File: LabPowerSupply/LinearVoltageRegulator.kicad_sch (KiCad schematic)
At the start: 16 parts, among them Q1_LVR1 PJA3404_R1_00001, Q2_LVR1 PJA3404_R1_00001, Q3_LVR1 PJA3404_R1_00001

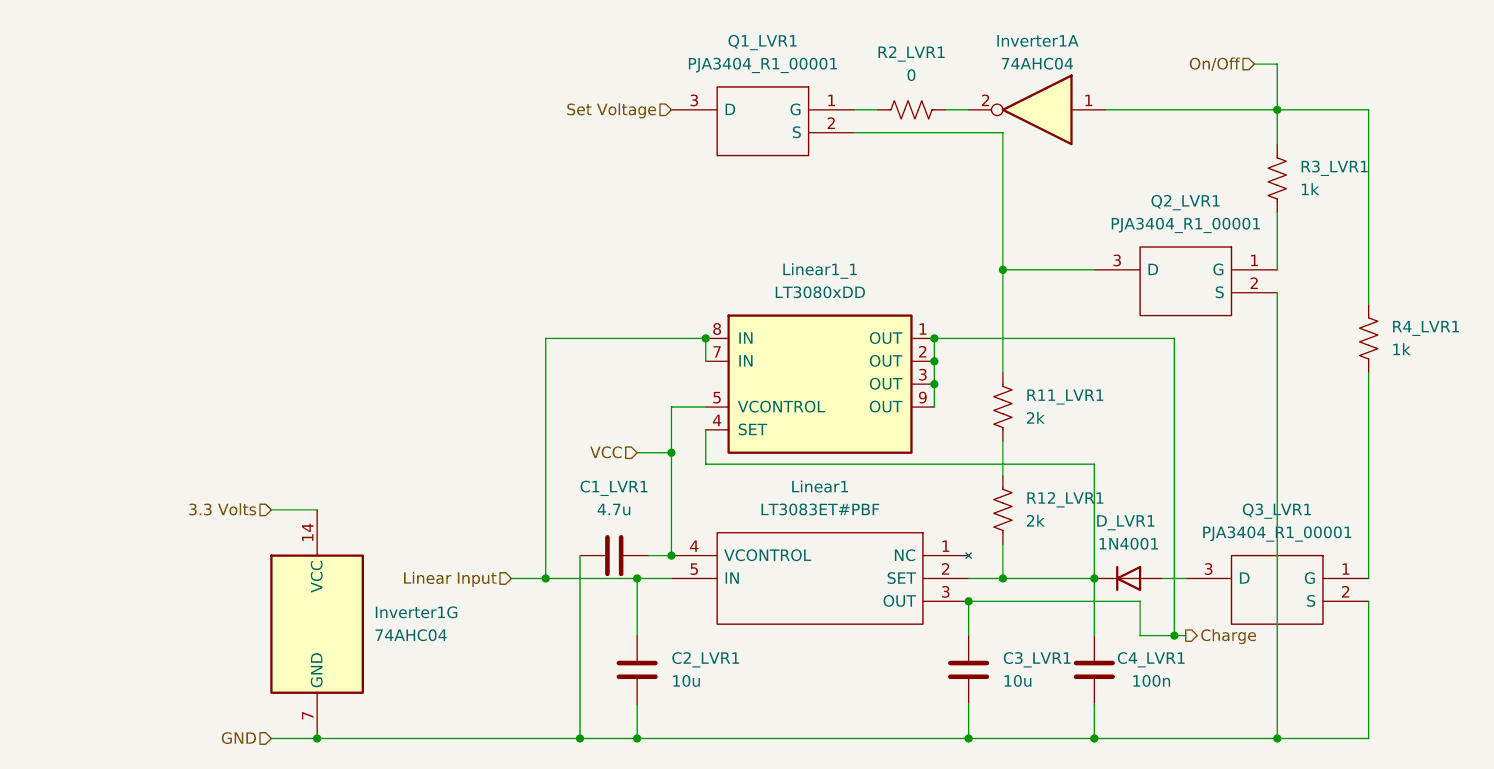
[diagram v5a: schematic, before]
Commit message: Changed capacitors to x7r
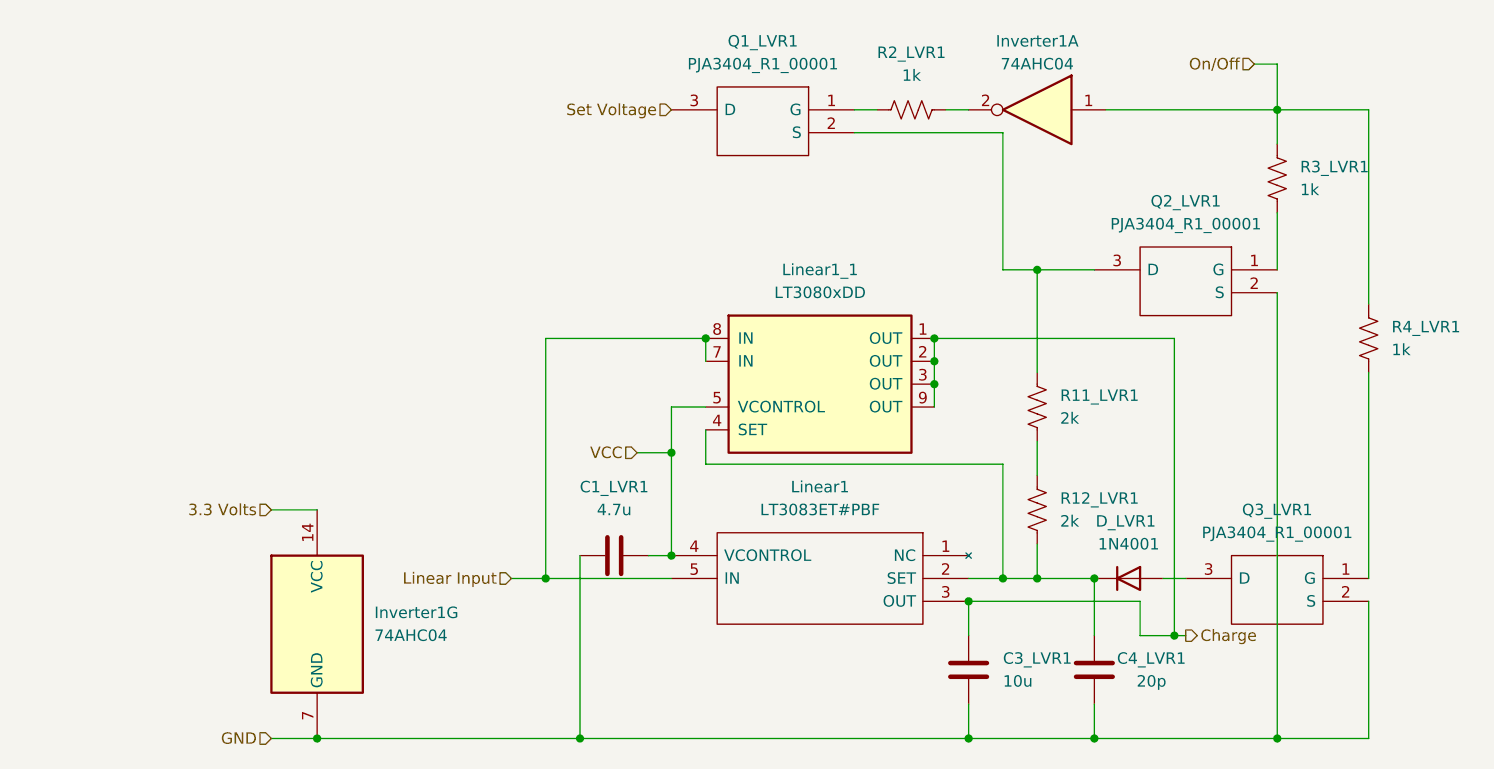
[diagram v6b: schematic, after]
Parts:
- removed C2_LVR1: 10u, Capacitor_SMD:C_0805_2012Metric, symbol Device:C
- C3_LVR1: footprint Capacitor_SMD:C_0805_2012Metric -> Capacitor_SMD:C_1210_3225Metric
- C4_LVR1: value 100n -> 20p
- R2_LVR1: value 0 -> 1k
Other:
- moved on the sheet: R11_LVR1, R12_LVR1
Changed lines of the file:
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@@
     (comment 4 "The linear voltage regulator is the main source for the power")
   )
+  (junction (at 177.8 87.63) (diameter 0) (color 0 0 0 0)
+  )
+  (junction (at 137.16 107.95) (diameter 0) (color 0 0 0 0)
+  )
   (junction (at 173.99 121.92) (diameter 0) (color 0 0 0 0)
   )
-  (junction (at 137.16 107.95) (diameter 0) (color 0 0 0 0)
-  )
   (junction (at 166.37 97.79) (diameter 0) (color 0 0 0 0)
   )
@@
   (junction (at 184.15 139.7) (diameter 0) (color 0 0 0 0)
   )
-  (junction (at 173.99 87.63) (diameter 0) (color 0 0 0 0)
-  )
   (junction (at 137.16 119.38) (diameter 0) (color 0 0 0 0)
   )
@@
   (junction (at 204.47 139.7) (diameter 0) (color 0 0 0 0)
   )
-  (junction (at 133.35 121.92) (diameter 0) (color 0 0 0 0)
-  )
   (junction (at 127 139.7) (diameter 0) (color 0 0 0 0)
   )
@@
   (junction (at 170.18 124.46) (diameter 0) (color 0 0 0 0)
   )
-  (junction (at 133.35 139.7) (diameter 0) (color 0 0 0 0)
+  (junction (at 177.8 121.92) (diameter 0) (color 0 0 0 0)
   )
   (junction (at 166.37 95.25) (diameter 0) (color 0 0 0 0)
@@
   (junction (at 166.37 100.33) (diameter 0) (color 0 0 0 0)
   )
-  (wire (pts (xy 133.35 139.7) (xy 170.18 139.7))
+  (wire (pts (xy 127 139.7) (xy 170.18 139.7))
     (stroke (width 0) (type default) (color 0 0 0 0))
   )
@@
     (stroke (width 0) (type default) (color 0 0 0 0))
   )
+  (wire (pts (xy 173.99 109.22) (xy 173.99 121.92))
+    (stroke (width 0) (type default) (color 0 0 0 0))
+  )
   (wire (pts (xy 140.97 95.25) (xy 140.97 97.79))
     (stroke (width 0) (type default) (color 0 0 0 0))
@@
     (stroke (width 0) (type default) (color 0 0 0 0))
   )
-  (wire (pts (xy 123.19 121.92) (xy 133.35 121.92))
+  (wire (pts (xy 177.8 121.92) (xy 184.15 121.92))
+    (stroke (width 0) (type default) (color 0 0 0 0))
+  )
+  (wire (pts (xy 123.19 121.92) (xy 137.16 121.92))
+    (stroke (width 0) (type default) (color 0 0 0 0))
+  )
+  (wire (pts (xy 177.8 87.63) (xy 184.15 87.63))
     (stroke (width 0) (type default) (color 0 0 0 0))
   )
@@
     (stroke (width 0) (type default) (color 0 0 0 0))
   )
-  (wire (pts (xy 184.15 121.92) (xy 184.15 109.22))
-    (stroke (width 0) (type default) (color 0 0 0 0))
-  )
   (wire (pts (xy 167.64 69.85) (xy 170.18 69.85))
     (stroke (width 0) (type default) (color 0 0 0 0))
   )
-  (wire (pts (xy 137.16 121.92) (xy 133.35 121.92))
-    (stroke (width 0) (type default) (color 0 0 0 0))
-  )
   (wire (pts (xy 214.63 69.85) (xy 214.63 91.44))
     (stroke (width 0) (type default) (color 0 0 0 0))
@@
     (stroke (width 0) (type default) (color 0 0 0 0))
   )
-  (wire (pts (xy 173.99 87.63) (xy 173.99 99.06))
-    (stroke (width 0) (type default) (color 0 0 0 0))
-  )
-  (wire (pts (xy 127 139.7) (xy 133.35 139.7))
+  (wire (pts (xy 177.8 87.63) (xy 177.8 99.06))
     (stroke (width 0) (type default) (color 0 0 0 0))
   )
@@
     (stroke (width 0) (type default) (color 0 0 0 0))
   )
-  (wire (pts (xy 133.35 121.92) (xy 133.35 128.27))
-    (stroke (width 0) (type default) (color 0 0 0 0))
-  )
   (wire (pts (xy 166.37 100.33) (xy 166.37 102.87))
     (stroke (width 0) (type default) (color 0 0 0 0))
   )
-  (wire (pts (xy 184.15 109.22) (xy 140.97 109.22))
-    (stroke (width 0) (type default) (color 0 0 0 0))
-  )
   (wire (pts (xy 166.37 95.25) (xy 166.37 97.79))
     (stroke (width 0) (type default) (color 0 0 0 0))
   )
+  (wire (pts (xy 140.97 109.22) (xy 173.99 109.22))
+    (stroke (width 0) (type default) (color 0 0 0 0))
+  )
   (wire (pts (xy 204.47 64.77) (xy 204.47 69.85))
     (stroke (width 0) (type default) (color 0 0 0 0))
@@
     (stroke (width 0) (type default) (color 0 0 0 0))
   )
-  (wire (pts (xy 173.99 121.92) (xy 184.15 121.92))
-    (stroke (width 0) (type default) (color 0 0 0 0))
-  )
   (wire (pts (xy 119.38 121.92) (xy 123.19 121.92))
     (stroke (width 0) (type default) (color 0 0 0 0))
   )
-  (wire (pts (xy 173.99 106.68) (xy 173.99 110.49))
+  (wire (pts (xy 177.8 106.68) (xy 177.8 110.49))
+    (stroke (width 0) (type default) (color 0 0 0 0))
+  )
+  (wire (pts (xy 177.8 87.63) (xy 173.99 87.63))
     (stroke (width 0) (type default) (color 0 0 0 0))
   )
@@
     (stroke (width 0) (type default) (color 0 0 0 0))
   )
-  (wire (pts (xy 173.99 87.63) (xy 184.15 87.63))
-    (stroke (width 0) (type default) (color 0 0 0 0))
-  )
   (wire (pts (xy 189.23 128.27) (xy 193.04 128.27))
     (stroke (width 0) (type default) (color 0 0 0 0))
@@
     (stroke (width 0) (type default) (color 0 0 0 0))
   )
-  (wire (pts (xy 173.99 118.11) (xy 173.99 121.92))
+  (wire (pts (xy 177.8 118.11) (xy 177.8 121.92))
     (stroke (width 0) (type default) (color 0 0 0 0))
   )
@@
     (stroke (width 0) (type default) (color 0 0 0 0))
   )
-  (wire (pts (xy 133.35 135.89) (xy 133.35 139.7))
+  (wire (pts (xy 173.99 121.92) (xy 177.8 121.92))
     (stroke (width 0) (type default) (color 0 0 0 0))
   )
@@
     (effects (font (size 1.27 1.27)) (justify right))
   )
-  (symbol (lib_id "Device:R_US") (at 173.99 114.3 180) (unit 1)
-    (in_bom yes) (on_board yes) (fields_autoplaced)
-    (property "Reference" "R12_LVR1" (id 0) (at 176.53 113.0299 0)
-      (effects (font (size 1.27 1.27)) (justify right))
-    )
-    (property "Value" "2k" (id 1) (at 176.53 115.5699 0)
-      (effects (font (size 1.27 1.27)) (justify right))
-    )
-    (property "Footprint" "Resistor_SMD:R_0603_1608Metric" (id 2) (at 172.974 114.046 90)
-      (effects (font (size 1.27 1.27)) hide)
-    )
-    (property "Datasheet" "~" (id 3) (at 173.99 114.3 0)
+  (symbol (lib_id "Device:R_US") (at 177.8 114.3 180) (unit 1)
+    (in_bom yes) (on_board yes) (fields_autoplaced)
+    (property "Reference" "R12_LVR1" (id 0) (at 180.34 113.0299 0)
+      (effects (font (size 1.27 1.27)) (justify right))
+    )
+    (property "Value" "2k" (id 1) (at 180.34 115.5699 0)
+      (effects (font (size 1.27 1.27)) (justify right))
+    )
+    (property "Footprint" "Resistor_SMD:R_0603_1608Metric" (id 2) (at 176.784 114.046 90)
+      (effects (font (size 1.27 1.27)) hide)
+    )
+    (property "Datasheet" "~" (id 3) (at 177.8 114.3 0)
       (effects (font (size 1.27 1.27)) hide)
     )
@@
     (in_bom yes) (on_board yes)
     (property "Reference" "C4_LVR1" (id 0) (at 190.5 130.81 0))
-    (property "Value" "100n" (id 1) (at 190.5 133.35 0))
+    (property "Value" "20p" (id 1) (at 190.5 133.35 0))
     (property "Footprint" "Capacitor_SMD:C_0603_1608Metric" (id 2) (at 185.1152 135.89 0)
       (effects (font (size 1.27 1.27)) hide)
@@
     (in_bom yes) (on_board yes) (fields_autoplaced)
     (property "Reference" "R2_LVR1" (id 0) (at 163.83 63.5 90))
-    (property "Value" "0" (id 1) (at 163.83 66.04 90))
+    (property "Value" "1k" (id 1) (at 163.83 66.04 90))
     (property "Footprint" "Resistor_SMD:R_0603_1608Metric" (id 2) (at 164.084 68.834 90)
       (effects (font (size 1.27 1.27)) hide)
@@
     (pin "2")
   )
-  (symbol (lib_id "Device:R_US") (at 173.99 102.87 180) (unit 1)
-    (in_bom yes) (on_board yes) (fields_autoplaced)
-    (property "Reference" "R11_LVR1" (id 0) (at 176.53 101.5999 0)
-      (effects (font (size 1.27 1.27)) (justify right))
-    )
-    (property "Value" "2k" (id 1) (at 176.53 104.1399 0)
-      (effects (font (size 1.27 1.27)) (justify right))
-    )
-    (property "Footprint" "Resistor_SMD:R_0603_1608Metric" (id 2) (at 172.974 102.616 90)
-      (effects (font (size 1.27 1.27)) hide)
-    )
-    (property "Datasheet" "~" (id 3) (at 173.99 102.87 0)
+  (symbol (lib_id "Device:R_US") (at 177.8 102.87 180) (unit 1)
+    (in_bom yes) (on_board yes) (fields_autoplaced)
+    (property "Reference" "R11_LVR1" (id 0) (at 180.34 101.5999 0)
+      (effects (font (size 1.27 1.27)) (justify right))
+    )
+    (property "Value" "2k" (id 1) (at 180.34 104.1399 0)
+      (effects (font (size 1.27 1.27)) (justify right))
+    )
+    (property "Footprint" "Resistor_SMD:R_0603_1608Metric" (id 2) (at 176.784 102.616 90)
+      (effects (font (size 1.27 1.27)) hide)
+    )
+    (property "Datasheet" "~" (id 3) (at 177.8 102.87 0)
       (effects (font (size 1.27 1.27)) hide)
     )
@@
     )
     (property "Datasheet" "~" (id 3) (at 204.47 77.47 0)
-      (effects (font (size 1.27 1.27)) hide)
-    )
-    (pin "1")
-    (pin "2")
-  )
-  (symbol (lib_id "Device:C") (at 133.35 132.08 0) (unit 1)
-    (in_bom yes) (on_board yes)
-    (property "Reference" "C2_LVR1" (id 0) (at 137.16 130.8099 0)
-      (effects (font (size 1.27 1.27)) (justify left))
-    )
-    (property "Value" "10u" (id 1) (at 137.16 133.3499 0)
-      (effects (font (size 1.27 1.27)) (justify left))
-    )
-    (property "Footprint" "Capacitor_SMD:C_0805_2012Metric" (id 2) (at 134.3152 135.89 0)
-      (effects (font (size 1.27 1.27)) hide)
-    )
-    (property "Datasheet" "~" (id 3) (at 133.35 132.08 0)
       (effects (font (size 1.27 1.27)) hide)
     )
@@
       (effects (font (size 1.27 1.27)) (justify left))
     )
-    (property "Footprint" "Capacitor_SMD:C_0805_2012Metric" (id 2) (at 171.1452 135.89 0)
-      (effects (font (size 1.27 1.27)) hide)
-    )
+    (property "Footprint" "Capacitor_SMD:C_1210_3225Metric" (id 2) (at 171.1452 135.89 0)
+      (effects (font (size 1.27 1.27)) hide)
+    )

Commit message: Fixed cap footprints
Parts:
- C3_LVR1: footprint Capacitor_SMD:C_1210_3225Metric -> Capacitor_SMD:C_1206_3216Metric
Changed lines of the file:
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@@
       (effects (font (size 1.27 1.27)) (justify left))
     )
-    (property "Footprint" "Capacitor_SMD:C_1210_3225Metric" (id 2) (at 171.1452 135.89 0)
+    (property "Footprint" "Capacitor_SMD:C_1206_3216Metric" (id 2) (at 171.1452 135.89 0)
       (effects (font (size 1.27 1.27)) hide)
     )

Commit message: SMD Oscillator
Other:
- moved on the sheet: C1_LVR1
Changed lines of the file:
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@@
   (junction (at 177.8 87.63) (diameter 0) (color 0 0 0 0)
   )
-  (junction (at 137.16 107.95) (diameter 0) (color 0 0 0 0)
-  )
   (junction (at 173.99 121.92) (diameter 0) (color 0 0 0 0)
   )
@@
   (junction (at 193.04 128.27) (diameter 0) (color 0 0 0 0)
   )
+  (junction (at 130.81 119.38) (diameter 0) (color 0 0 0 0)
+  )
   (junction (at 170.18 139.7) (diameter 0) (color 0 0 0 0)
   )
   (junction (at 204.47 139.7) (diameter 0) (color 0 0 0 0)
   )
-  (junction (at 127 139.7) (diameter 0) (color 0 0 0 0)
+  (junction (at 130.81 139.7) (diameter 0) (color 0 0 0 0)
   )
   (junction (at 123.19 121.92) (diameter 0) (color 0 0 0 0)
@@
   (junction (at 166.37 100.33) (diameter 0) (color 0 0 0 0)
   )
-  (wire (pts (xy 127 139.7) (xy 170.18 139.7))
+  (wire (pts (xy 97.79 139.7) (xy 130.81 139.7))
     (stroke (width 0) (type default) (color 0 0 0 0))
   )
@@
     (stroke (width 0) (type default) (color 0 0 0 0))
   )
-  (wire (pts (xy 127 119.38) (xy 127 139.7))
-    (stroke (width 0) (type default) (color 0 0 0 0))
-  )
   (wire (pts (xy 170.18 121.92) (xy 173.99 121.92))
     (stroke (width 0) (type default) (color 0 0 0 0))
@@
     (stroke (width 0) (type default) (color 0 0 0 0))
   )
-  (wire (pts (xy 133.35 107.95) (xy 137.16 107.95))
-    (stroke (width 0) (type default) (color 0 0 0 0))
-  )
   (wire (pts (xy 170.18 139.7) (xy 184.15 139.7))
     (stroke (width 0) (type default) (color 0 0 0 0))
@@
     (stroke (width 0) (type default) (color 0 0 0 0))
   )
+  (wire (pts (xy 129.54 119.38) (xy 130.81 119.38))
+    (stroke (width 0) (type default) (color 0 0 0 0))
+  )
   (wire (pts (xy 170.18 135.89) (xy 170.18 139.7))
     (stroke (width 0) (type default) (color 0 0 0 0))
@@
     (stroke (width 0) (type default) (color 0 0 0 0))
   )
-  (wire (pts (xy 134.62 119.38) (xy 137.16 119.38))
+  (wire (pts (xy 130.81 139.7) (xy 170.18 139.7))
+    (stroke (width 0) (type default) (color 0 0 0 0))
+  )
+  (wire (pts (xy 130.81 119.38) (xy 137.16 119.38))
     (stroke (width 0) (type default) (color 0 0 0 0))
   )
@@
     (stroke (width 0) (type default) (color 0 0 0 0))
   )
+  (wire (pts (xy 130.81 134.62) (xy 130.81 139.7))
+    (stroke (width 0) (type default) (color 0 0 0 0))
+  )
   (wire (pts (xy 177.8 106.68) (xy 177.8 110.49))
     (stroke (width 0) (type default) (color 0 0 0 0))
@@
     (stroke (width 0) (type default) (color 0 0 0 0))
   )
-  (wire (pts (xy 137.16 107.95) (xy 137.16 102.87))
-    (stroke (width 0) (type default) (color 0 0 0 0))
-  )
   (wire (pts (xy 189.23 128.27) (xy 193.04 128.27))
     (stroke (width 0) (type default) (color 0 0 0 0))
   )
-  (wire (pts (xy 97.79 139.7) (xy 127 139.7))
-    (stroke (width 0) (type default) (color 0 0 0 0))
-  )
   (wire (pts (xy 204.47 139.7) (xy 214.63 139.7))
     (stroke (width 0) (type default) (color 0 0 0 0))
@@
     (stroke (width 0) (type default) (color 0 0 0 0))
   )
-  (wire (pts (xy 137.16 107.95) (xy 137.16 119.38))
+  (wire (pts (xy 137.16 102.87) (xy 137.16 119.38))
     (stroke (width 0) (type default) (color 0 0 0 0))
   )
@@
   )
   (wire (pts (xy 123.19 121.92) (xy 123.19 95.25))
+    (stroke (width 0) (type default) (color 0 0 0 0))
+  )
+  (wire (pts (xy 130.81 119.38) (xy 130.81 127))
     (stroke (width 0) (type default) (color 0 0 0 0))
   )
@@
     (effects (font (size 1.27 1.27)) (justify right))
   )
-  (hierarchical_label "VCC" (shape input) (at 133.35 107.95 180)
+  (hierarchical_label "VCC" (shape input) (at 129.54 119.38 180)
     (effects (font (size 1.27 1.27)) (justify right))
   )
@@
     (pin "5")
   )
-  (symbol (lib_id "Device:C") (at 130.81 119.38 90) (unit 1)
-    (in_bom yes) (on_board yes) (fields_autoplaced)
-    (property "Reference" "C1_LVR1" (id 0) (at 130.81 111.76 90))
-    (property "Value" "4.7u" (id 1) (at 130.81 114.3 90))
-    (property "Footprint" "Capacitor_SMD:C_0805_2012Metric" (id 2) (at 134.62 118.4148 0)
-      (effects (font (size 1.27 1.27)) hide)
-    )
-    (property "Datasheet" "~" (id 3) (at 130.81 119.38 0)
-      (effects (font (size 1.27 1.27)) hide)
-    )
+  (symbol (lib_id "Device:C") (at 130.81 130.81 180) (unit 1)
+    (in_bom yes) (on_board yes) (fields_autoplaced)
+    (property "Reference" "C1_LVR1" (id 0) (at 134.62 129.5399 0)
+      (effects (font (size 1.27 1.27)) (justify right))
+    )
+    (property "Value" "4.7u" (id 1) (at 134.62 132.0799 0)
+      (effects (font (size 1.27 1.27)) (justify right))
+    )
+    (property "Footprint" "Capacitor_SMD:C_0805_2012Metric" (id 2) (at 129.8448 127 0)
+      (effects (font (size 1.27 1.27)) hide)
+    )
+    (property "Datasheet" "~" (id 3) (at 130.81 130.81 0)
+      (effects (font (size 1.27 1.27)) hide)
+    )
